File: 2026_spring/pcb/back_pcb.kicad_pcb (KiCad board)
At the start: 2 copper layers, 68 x 88.9 mm, 20 parts, among them J1 front joystick, J2 bottom joystick, J3 Arduino, J4 Arduino, SW1 Left Trigger, SW10 Home, SW11 Start, SW13 A, SW14 X, SW15 Y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

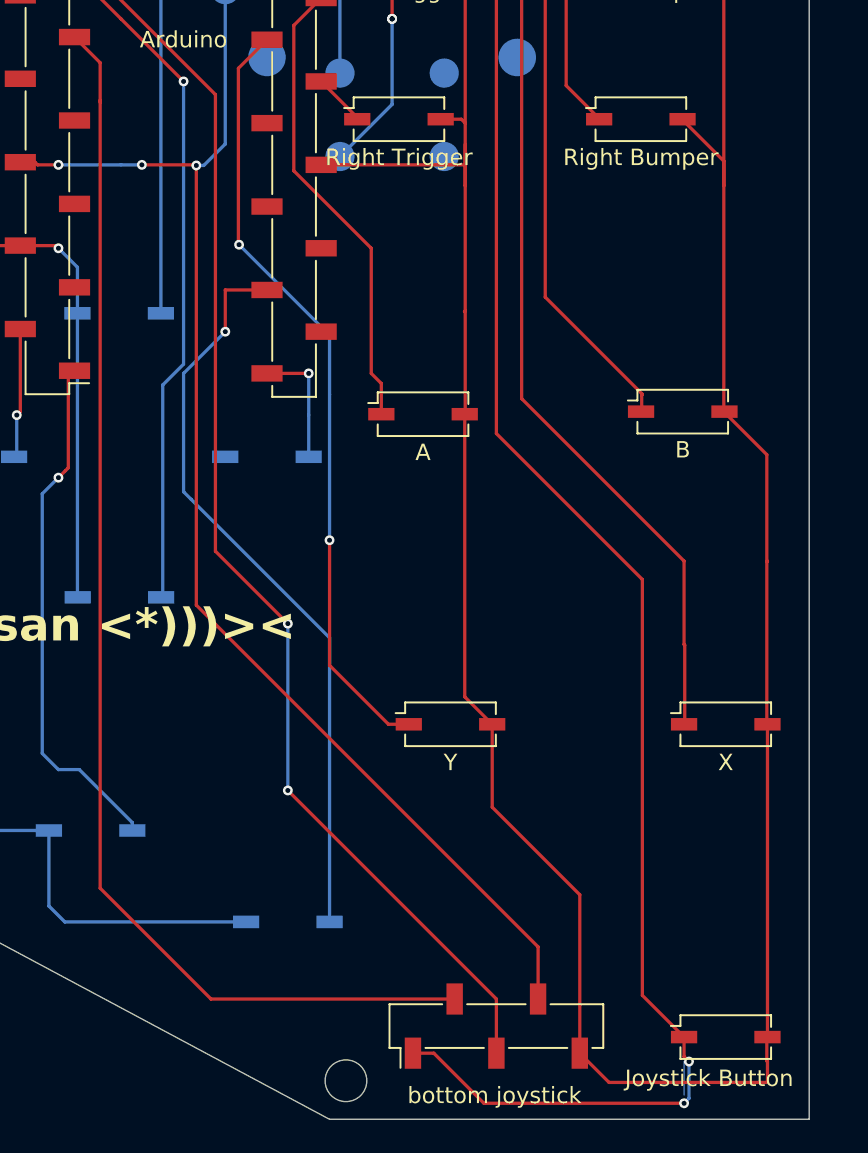
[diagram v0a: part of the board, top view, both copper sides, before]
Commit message: :construction: fix screw terminals
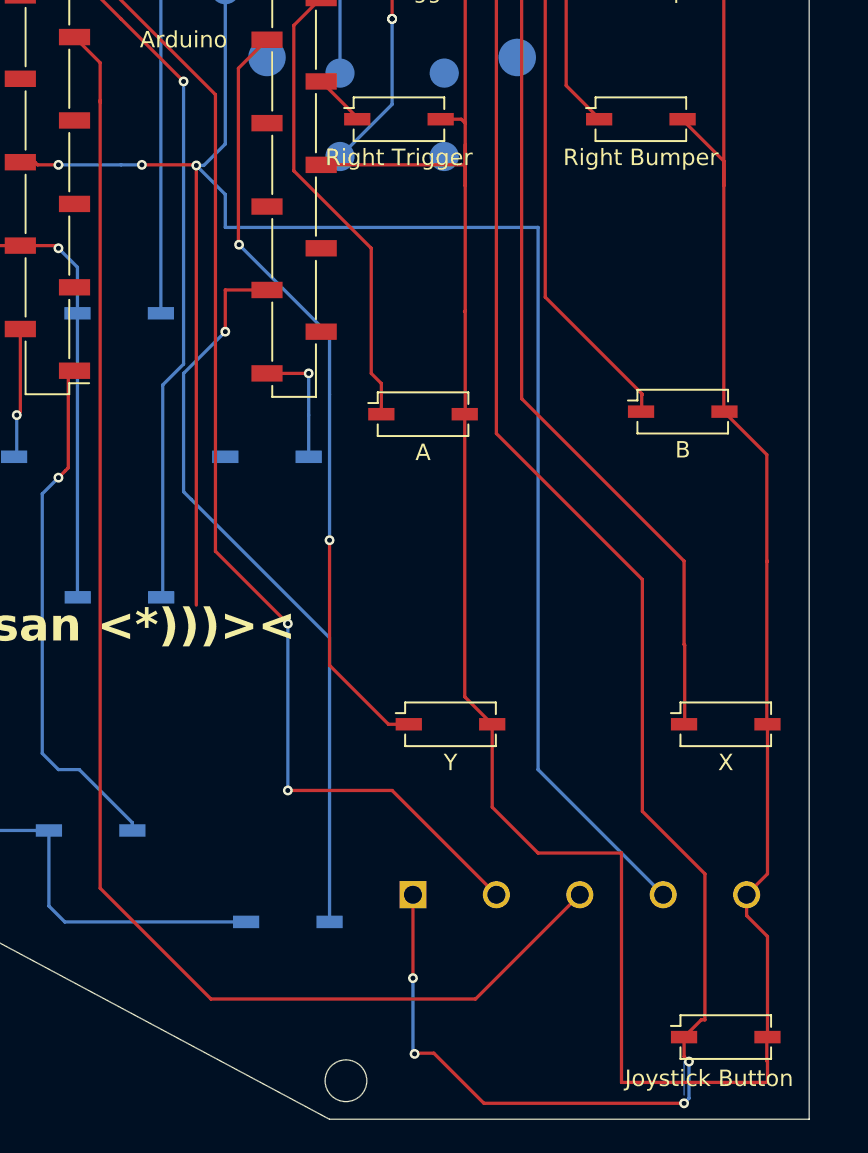
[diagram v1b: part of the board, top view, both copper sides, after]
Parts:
- J2: footprint Connector_PinSocket_2.54mm:PinSocket_1x05_P2.54mm_Vertical_SMD_Pin1Left -> Downloads:TE_282837-5; moved to B.Cu
- moved J2 9.48 mm to (97.8, 121.9), turned to 0 degrees
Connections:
- J2 pad 2: /A5 -> /A3
- J2 pad 3: /A3 -> /A5
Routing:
- net /VCC: track 105.6 -> 140.3 mm
- net /D8: track 114.8 -> 125.7 mm, vias 2 -> 4
- net /A5: track 77.0 -> 87.2 mm
- net /A3: track 77.6 -> 71.7 mm
- net /GND: track 303.5 -> 307.1 mm

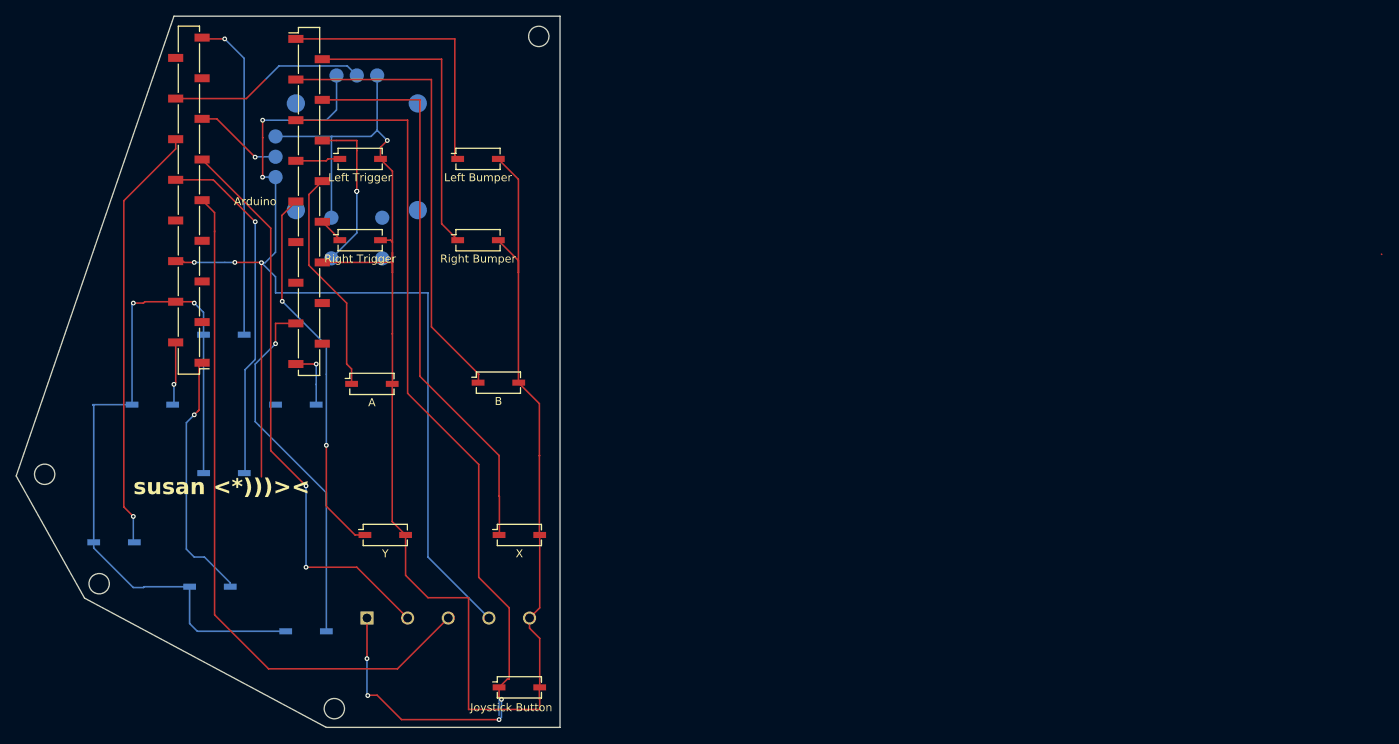
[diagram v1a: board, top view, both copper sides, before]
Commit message: :sparkle: move arduino to middle of pcb
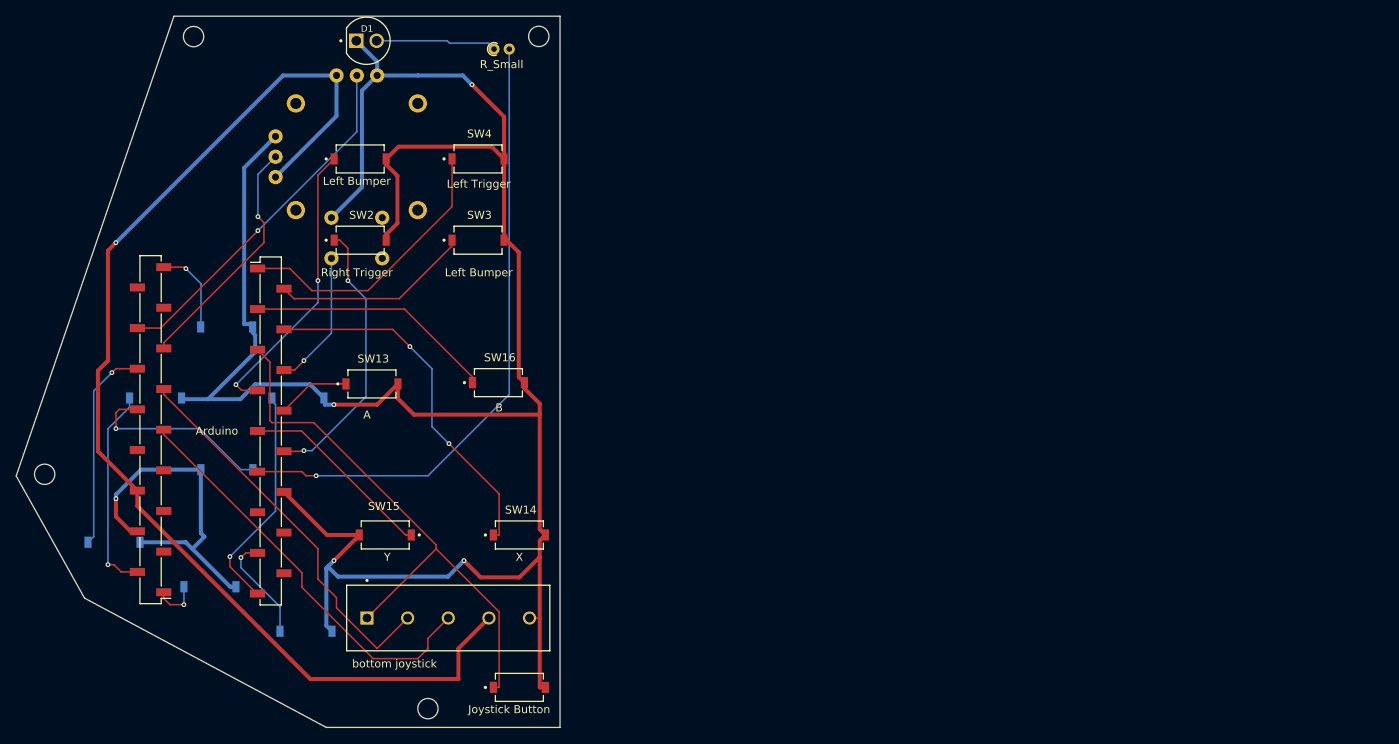
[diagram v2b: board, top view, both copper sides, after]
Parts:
- added D1: LED, Downloads:LEDRD254W57D500H1070, F.Cu at (87.6, 49.8)
- added R1: R_Small, Resistor_THT:R_Axial_DIN0204_L3.6mm_D1.6mm_P1.90mm_Vertical, F.Cu at (103.5, 50.8)
- J1: value front joystick -> Front Joystick
- J2: moved to F.Cu
- SW1, SW10, SW11, SW13, SW14, SW15, SW16, SW17, SW2, SW4, SW5, SW6, SW8, SW9: footprint Button_Switch_SMD:SW_DIP_SPSTx01_Slide_Copal_CHS-01A_W5.08mm_P1.27mm_JPin -> Downloads:SW_PTS636_SM43J_SMTR_LFS
- SW3: value Right Bumper -> Left Bumper; footprint Button_Switch_SMD:SW_DIP_SPSTx01_Slide_Copal_CHS-01A_W5.08mm_P1.27mm_JPin -> Downloads:SW_PTS636_SM43J_SMTR_LFS
- joy_SW: renamed from SW7; footprint Button_Switch_SMD:SW_DIP_SPSTx01_Slide_Copal_CHS-01A_W5.08mm_P1.27mm_JPin -> Downloads:SW_PTS636_SM43J_SMTR_LFS
- moved J3 29.1 mm to (75.6, 98.5)
- moved J4 29.1 mm to (60.6, 98.4)
- moved SW5 1.04 mm to (70.1, 85.5), turned to 0 degrees
- moved SW8 0.92 mm to (61.2, 94.4), turned to 0 degrees
- moved SW9 0.87 mm to (79.0, 94.4), turned to 0 degrees
- moved SW6 0.56 mm to (70.1, 103.4)
- turned SW10 to 0 degrees
- turned SW11 to 0 degrees
- turned SW15 to 180 degrees
- turned SW17 to 0 degrees
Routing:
- net /D2: track 0.00 -> 79.1 mm, vias 0 -> 1
- net /D8: track 125.7 -> 70.7 mm, vias 4 -> 0
- net /A5: track 87.2 -> 51.7 mm
- net /D1: track 45.8 -> 13.5 mm
- net /D3: track 3.21 -> 34.7 mm, vias 0 -> 2
- net /D6: track 5.60 -> 36.3 mm, vias 0 -> 2
- net /D13: track 40.9 -> 11.1 mm
- net /A2: track 53.6 -> 25.8 mm
- net /GND: track 307.1 -> 334.5 mm, vias 3 -> 5
- net /D10: track 58.1 -> 31.1 mm
- net /D15: track 31.8 -> 5.87 mm
- net /D9: track 71.5 -> 45.5 mm, vias 0 -> 2
- net /D4: track 47.5 -> 24.6 mm, vias 2 -> 0
- net /A3: track 71.7 -> 48.9 mm, vias 2 -> 0
- net /D16: track 7.13 -> 28.5 mm
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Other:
- outline, holes or cut-outs redrawn
- board text removed: "susan <*)))><"
